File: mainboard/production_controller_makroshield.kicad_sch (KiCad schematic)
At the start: 57 parts, among them J1 CON_TERM_BLK_1X2_TB008A-508-0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, J2 CON_TERM_BLK_1X2_TB008A-508-0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, J3 CON_HDR_MIKROBUS_ADDON_TH, J4 CON_TERM_BLK_1X2_TB008A-508-0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, J5 CON_HDR_MIKROBUS_SOCKET_TH, Q1 TRX_PMOS_AOD4189, Q2 TRX_2NPN_BC846S,115, U1 IO_EXP_PI4IOE5V6416ZDEX, U2 IO_EXP_PI4IOE5V6416ZDEX, U3 SUN_CUR_ACS711KEXLT-31AB-T, U4 ADC_NAU7802SGI

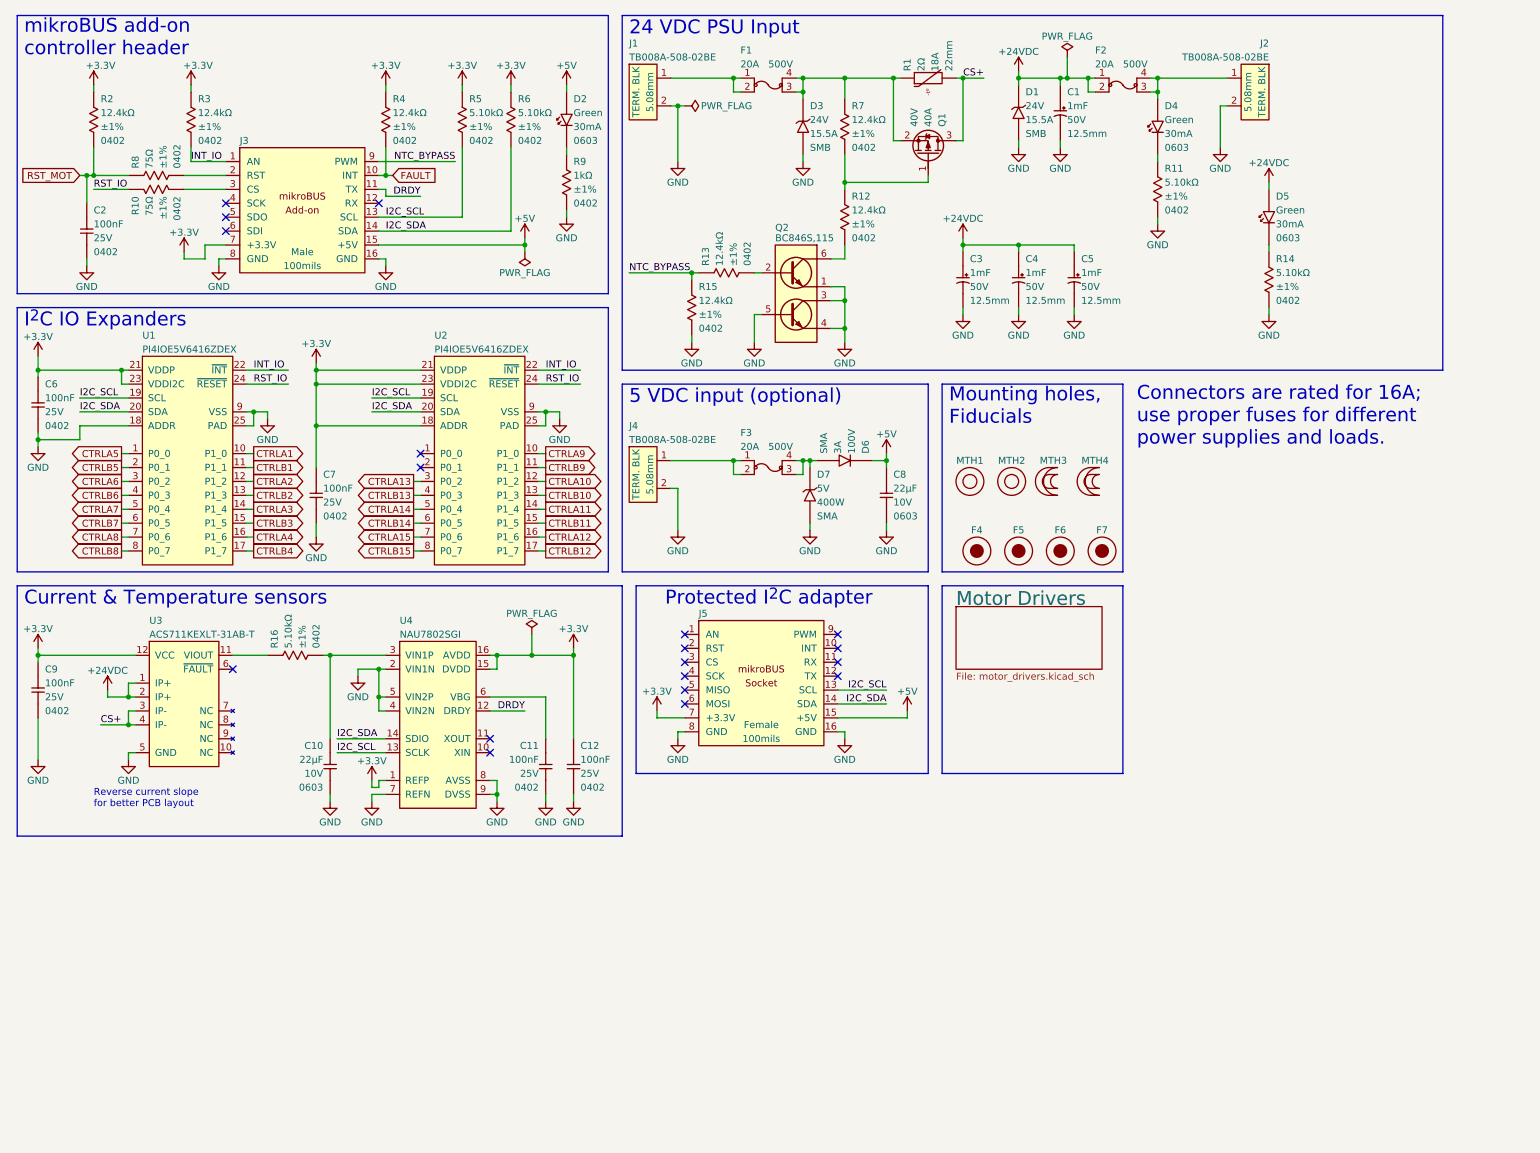
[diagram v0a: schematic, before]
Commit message: Invert connectors (male/female) Replace TH connectors with SMD ones on mainboard Add 555 timer on simple-switch to generate 60 Hz Add jumper on simple-switch to select AC Add series I2C resistors on mainboard from mikroBUS socket
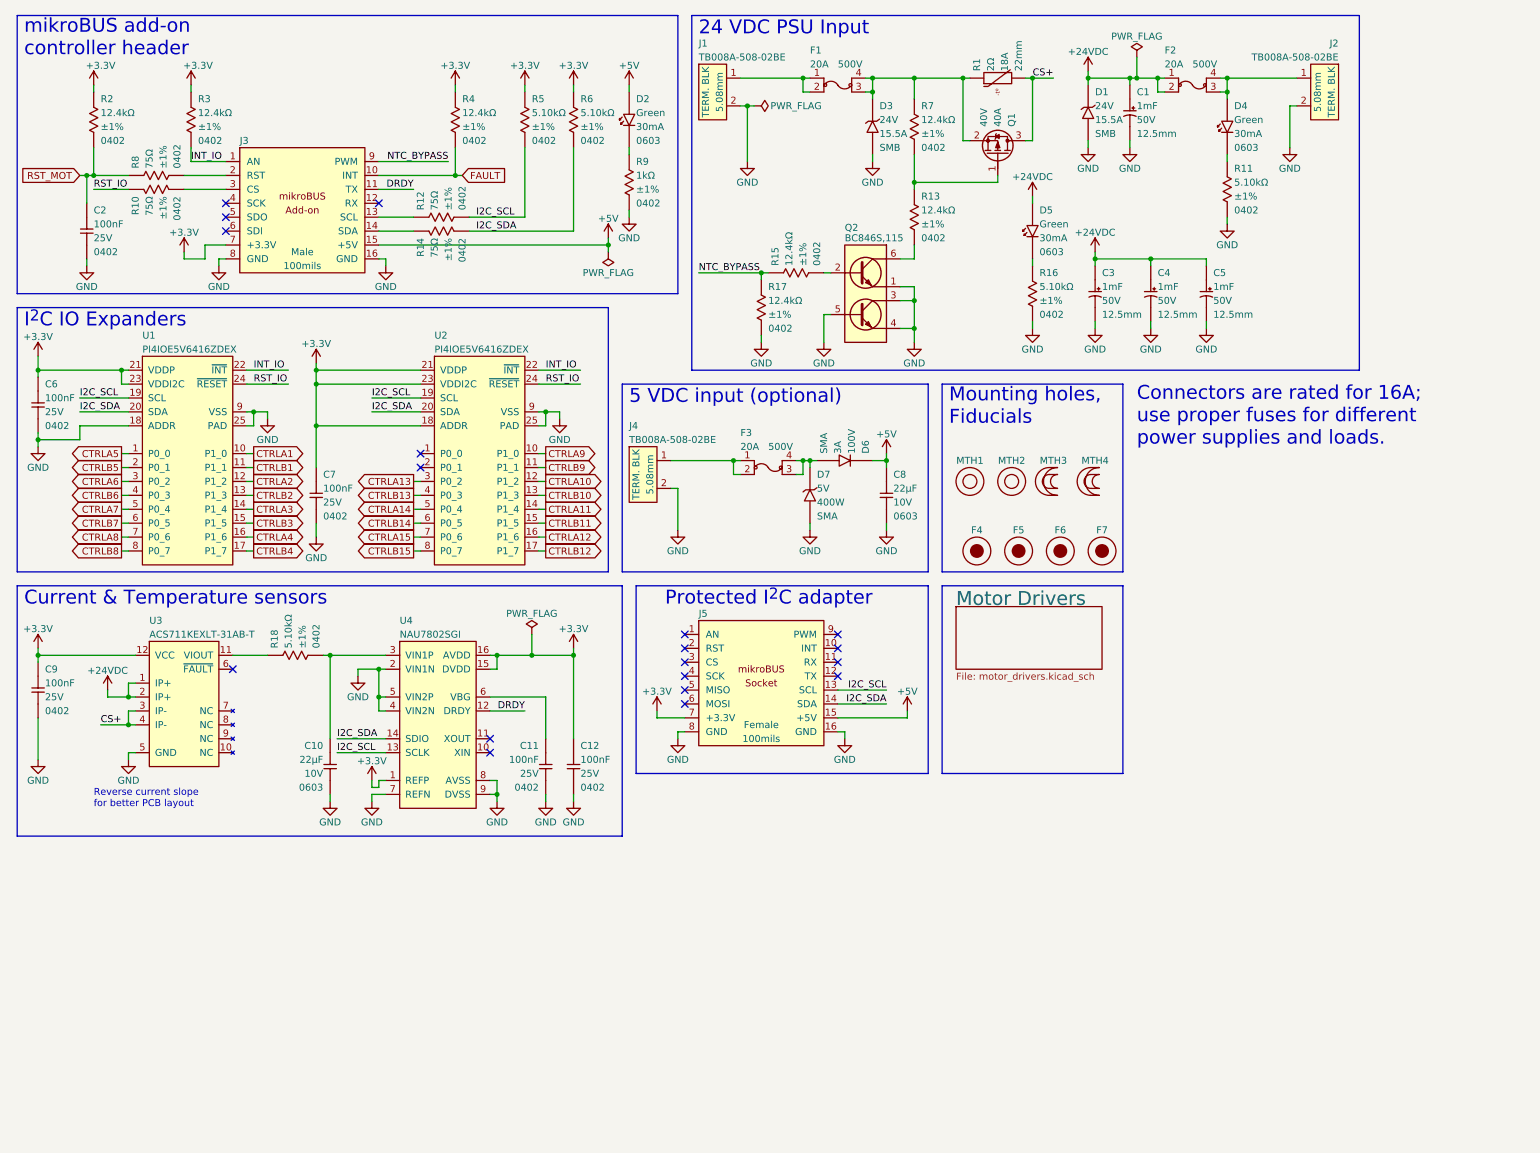
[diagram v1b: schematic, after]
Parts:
- added R12, R14: RES_226Ω_1%_0402, connaxio-resistors:RES_0402_1005M, symbol connaxio-resistors:RES_75Ω_1%_0402
- renumbered R12 to R13, R13 to R15, R14 to R16, R15 to R17, R16 to R18
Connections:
- net I2C_SCL: now also R12.2; no longer J3.13 (SCL)
- net I2C_SDA: now also R14.2; no longer J3.14 (SDA)
- new net: J3.14 (SDA), R14.1
- new net: J3.13 (SCL), R12.1
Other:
- moved on the sheet: C1, C3, C4, C5, D1, D2, D3, D4, D5, F1, F2, J1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

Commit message: Add onboard temperature sensor Add connector for Analog / 1-wire / PWM sensor
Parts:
- removed D4: DIO_LED_GREEN_150060GS75000, connaxio-diodes:LED_0603_1608M, symbol connaxio-diodes:DIO_LED_GREEN_150060GS75000
- removed R11: RES_5.10KΩ_1%_0402, connaxio-resistors:RES_0402_1005M, symbol connaxio-resistors:RES_5.10KΩ_1%_0402
- added C11: CAP_CER_22UF_10V_0603, connaxio-capacitors:CAP_CER_0603_1608M, symbol connaxio-capacitors:CAP_CER_22UF_10V_0603
- added C9: CAP_CER_100NF_25V_0402, connaxio-capacitors:CAP_CER_0402_1005M, symbol connaxio-capacitors:CAP_CER_100NF_25V_0402
- added D5: DIO_LED_GREEN_150060GS75000, connaxio-diodes:LED_0603_1608M, symbol connaxio-diodes:DIO_LED_GREEN_150060GS75000
- added J6: CON_HDR_100MILS_M_TH_1X3, connaxio-connectors:CON_HDR_100MILS_M_TH_1X3, symbol connaxio-connectors:CON_HDR_100MILS_M_TH_1X3
- added R16: PTC_SMD1210B010TF, connaxio-resistors:RES_1210_3225M, symbol connaxio-resistors:PTC_SMD1210B010TF
- added R17: RES_226Ω_1%_0402, connaxio-resistors:RES_0402_1005M, symbol connaxio-resistors:RES_75Ω_1%_0402
- added R18: RES_5.10KΩ_1%_0402, connaxio-resistors:RES_0402_1005M, symbol connaxio-resistors:RES_5.10KΩ_1%_0402
- added U3: SEN_TEMP_TMP1075DR, connaxio-sop:SOIC-8_3.9x4.9_P1.27, symbol connaxio-ic:SEN_TEMP_TMP1075DR
- U4: renamed from U3; value SUN_CUR_ACS711KEXLT-31AB-T -> SEN_CUR_ACS711KEXLT-31AB-T; symbol connaxio-ic:SUN_CUR_ACS711KEXLT-31AB-T -> connaxio-ic:SEN_CUR_ACS711KEXLT-31AB-T
- renumbered C9 to C10, C10 to C12, C11 to C13, C12 to C14, D3 to D2, D6 to D3, D7 to D4, D2 to D6, D5 to D7, R12 to R10, R13 to R11, R14 to R12, R15 to R13, R17 to R14, R18 to R15, R9 to R19, R16 to R20, R10 to R9, U4 to U5
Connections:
- net +3.3V: now also C9.1, R16.1, U3.8 (V+)
- net GND: now also C11.2, C9.2, J6.3, R18.2, U3.4 (GND), U3.5 (A2), U3.6 (A1), U3.7 (A0)
- net I2C_SCL: now also U3.2 (SCL)
- net I2C_SDA: now also U3.1 (SDA)
- net 24V_OUT: now reaches F2.3, F2.4, J2.1
- net 24V_OUT: now also D5.2 (A)
- net ONE_WIRE: now reaches J3.4 (SCK)
- net ONE_WIRE: now also R17.1
- new net: C11.1, J6.1, R16.2
- new net: J6.2, R17.2
- new net: D5.1 (K), R18.1
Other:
- note added: "1-wire / analog"
- note added: "Connector for external sensor"
- note added: "Fuse indicator LEDs"
- note added: "Fuse: 15A MAX"
- note added: "Fuse: <= F1"
- note added: "Onboard temp. sens."
- note removed: "Connectors are rated for 16A; use proper fuses for different power supplies and loads."
- moved on the sheet: C1, C2, C3, C4, C5, D1, D2, D6, D7, F1, F2, J1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

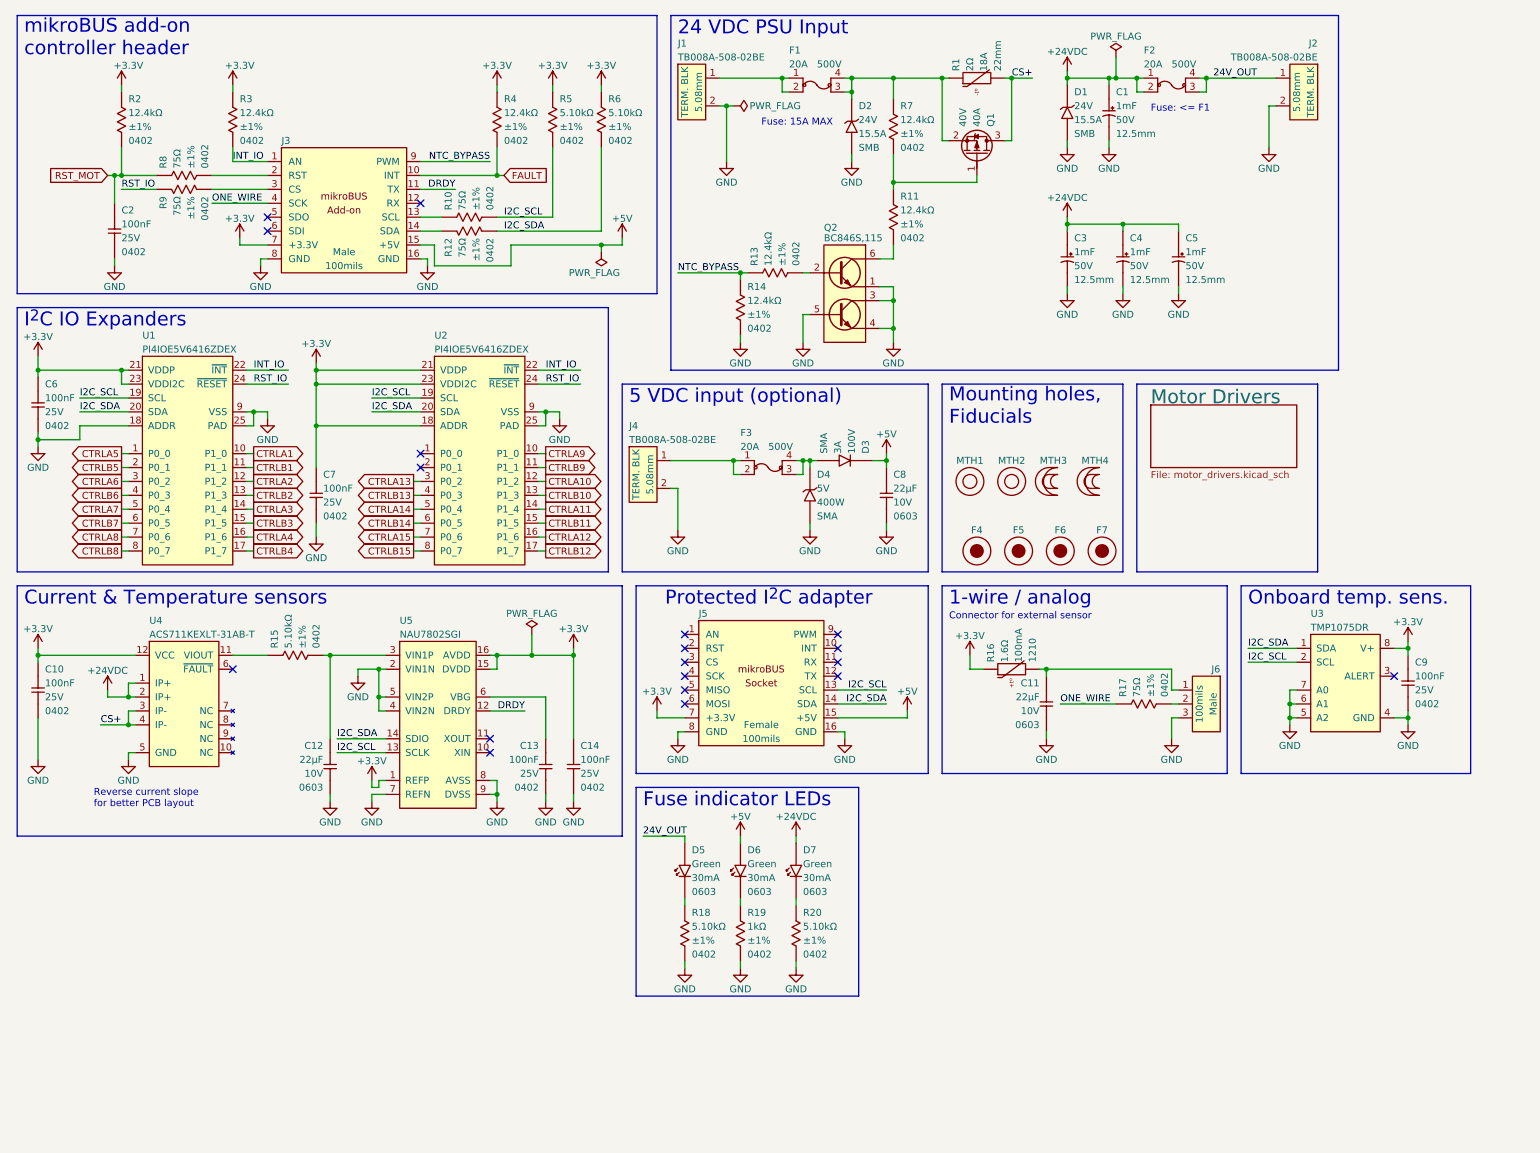
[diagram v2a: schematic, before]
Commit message: Add filter cap to current reading ADC
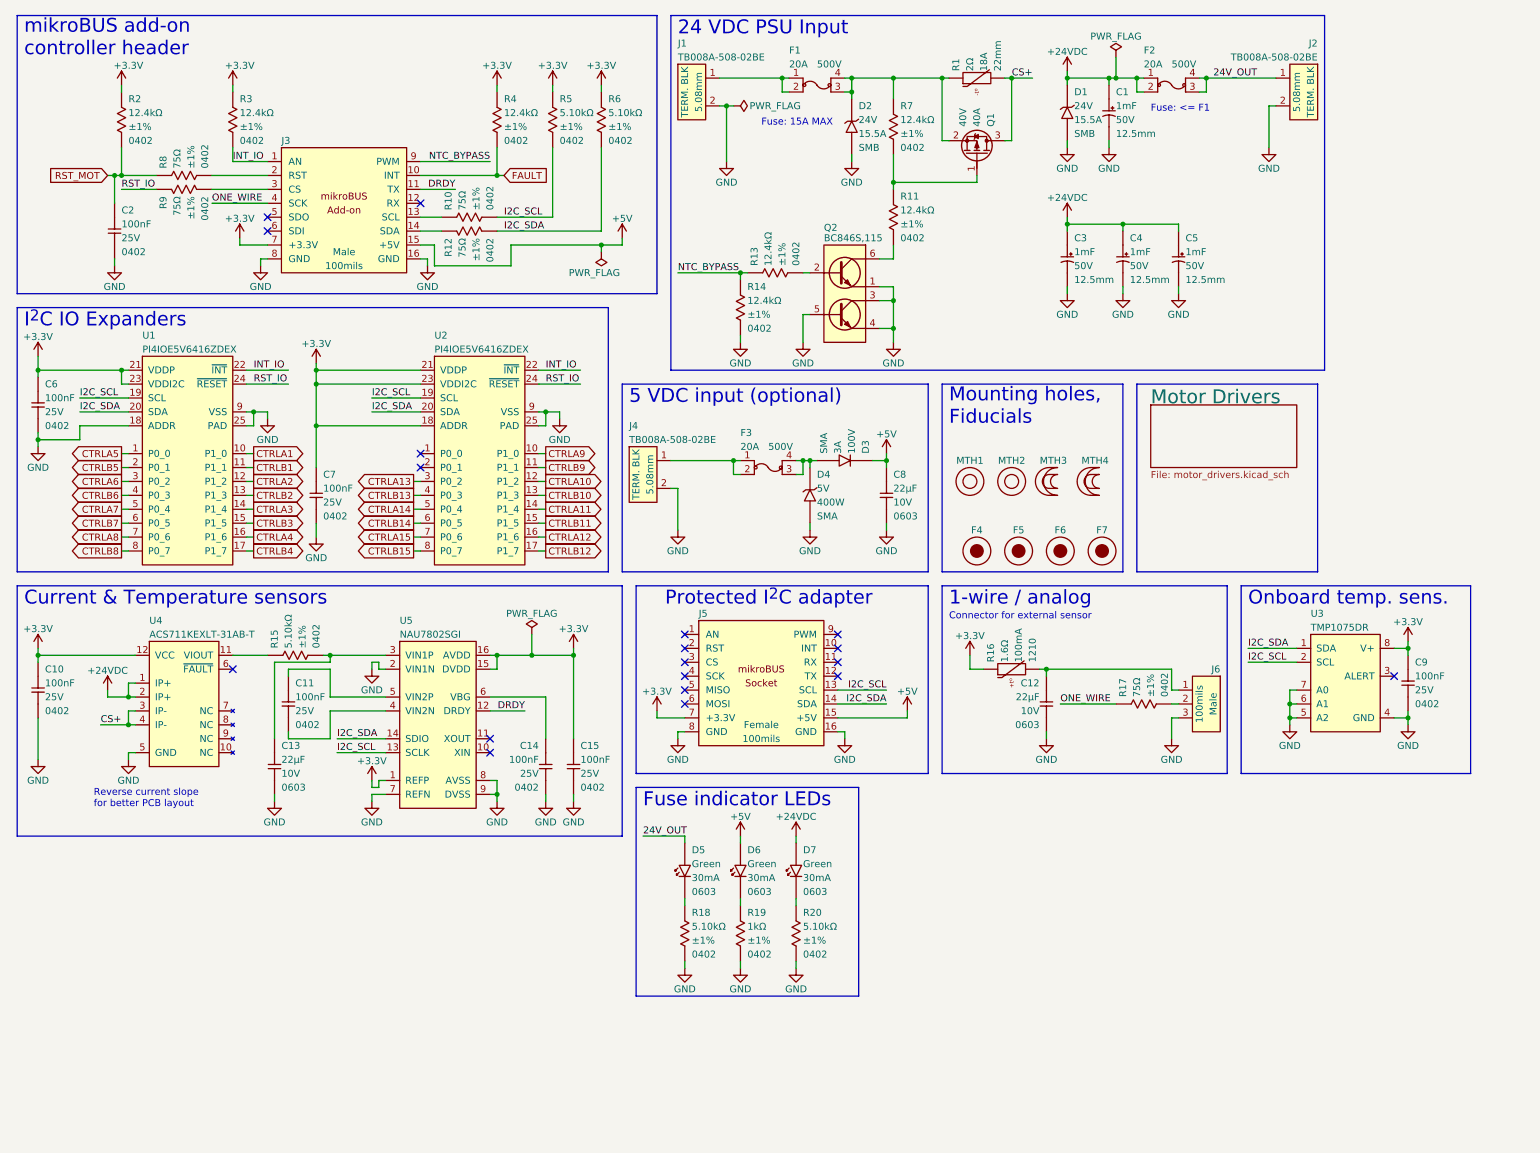
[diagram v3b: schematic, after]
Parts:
- added C11: CAP_CER_100NF_25V_0402, connaxio-capacitors:CAP_CER_0402_1005M, symbol connaxio-capacitors:CAP_CER_100NF_25V_0402
- renumbered C11 to C12, C12 to C13, C13 to C14, C14 to C15
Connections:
- net GND: no longer U5.4 (VIN2N), U5.5 (VIN2P)
- new net: C11.2, U5.4 (VIN2N)
- new net: C11.1, U5.5 (VIN2P)
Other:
- moved on the sheet: C13
